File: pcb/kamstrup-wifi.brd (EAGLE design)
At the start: 36 x 42.5 mm, 2 parts

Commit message: pcb: better aligning
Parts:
- moved JP1 9.08 mm to (4.00, 36.3)
- moved U$1 1.80 mm to (5.08, 14.0)
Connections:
- new net N$1: JP1.6, U$1.P$1
- new net N$2: JP1.4, U$1.P$5
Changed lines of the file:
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@@
 <layer number="43" name="vRestrict" color="2" fill="10" visible="yes" active="yes"/>
 <layer number="44" name="Drills" color="7" fill="1" visible="no" active="yes"/>
-<layer number="45" name="Holes" color="7" fill="1" visible="no" active="yes"/>
+<layer number="45" name="Holes" color="7" fill="1" visible="yes" active="yes"/>
 <layer number="46" name="Milling" color="3" fill="1" visible="no" active="yes"/>
 <layer number="47" name="Measures" color="7" fill="1" visible="no" active="yes"/>
@@
 <wire x1="36" y1="42.5" x2="0" y2="42.5" width="0" layer="20"/>
 <wire x1="0" y1="42.5" x2="0" y2="0" width="0" layer="20"/>
-<text x="5.08" y="24.13" size="1.778" layer="1" rot="R90" align="center-right">GND</text>
-<text x="7.62" y="24.13" size="1.778" layer="1" rot="R90" align="center-right">A</text>
-<text x="10.16" y="24.13" size="1.778" layer="1" rot="R90" align="center-right">B</text>
-<text x="5.08" y="31.75" size="1.778" layer="1" rot="R90" align="center-left">VCC</text>
-<text x="7.62" y="31.75" size="1.778" layer="1" rot="R90" align="center-left">TxD</text>
-<text x="10.16" y="31.75" size="1.778" layer="1" rot="R90" align="center-left">RxD</text>
+<text x="1.46" y="32.75" size="0.8128" layer="1" rot="R90" align="center-right">GND</text>
+<text x="4" y="32.75" size="0.8128" layer="1" rot="R90" align="center-right">A</text>
+<text x="6.54" y="32.75" size="0.8128" layer="1" rot="R90" align="center-right">B</text>
+<text x="1.46" y="39.37" size="0.8128" layer="1" rot="R90" align="center-left">VCC</text>
+<text x="4" y="39.37" size="0.8128" layer="1" rot="R90" align="center-left">TxD</text>
+<text x="6.54" y="39.37" size="0.8128" layer="1" rot="R90" align="center-left">RxD</text>
+<hole x="1.5" y="14" drill="2"/>
+<hole x="21.5" y="38.6" drill="2"/>
 </plain>
 <attributes>
@@
 </autorouter>
 <elements>
-<element name="JP1" library="SparkFun-Connectors" package="2X03" value="" x="7.62" y="27.94"/>
-<element name="U$1" library="ESP8266" package="ESP-01" value="ESP8266-01" x="6.35" y="15.24" rot="R270"/>
+<element name="JP1" library="SparkFun-Connectors" package="2X03" value="" x="4" y="36.27"/>
+<element name="U$1" library="ESP8266" package="ESP-01" value="ESP8266-01" x="5.08" y="13.97" rot="R270"/>
 </elements>
 <signals>
@@
 <contactref element="JP1" pad="1"/>
 <contactref element="U$1" pad="P$8"/>
-<wire x1="8.89" y1="15.24" x2="5.08" y2="26.67" width="0" layer="19" extent="1-1"/>
+<wire x1="7.62" y1="13.97" x2="1.46" y2="35" width="0" layer="19" extent="1-1"/>
 </signal>
 <signal name="3.3V">
 <contactref element="JP1" pad="2"/>
 <contactref element="U$1" pad="P$4"/>
-<wire x1="6.35" y1="7.62" x2="5.08" y2="29.21" width="0" layer="19" extent="1-1"/>
+<wire x1="5.08" y1="6.35" x2="1.46" y2="37.54" width="0" layer="19" extent="1-1"/>
+</signal>
+<signal name="N$1">
+<contactref element="U$1" pad="P$1"/>
+<contactref element="JP1" pad="6"/>
+<wire x1="5.08" y1="13.97" x2="6.54" y2="37.54" width="0" layer="19" extent="1-1"/>
+</signal>
+<signal name="N$2">
+<contactref element="JP1" pad="4"/>
+<contactref element="U$1" pad="P$5"/>
+<wire x1="7.62" y1="6.35" x2="4" y2="37.54" width="0" layer="19" extent="1-1"/>
 </signal>
 </signals>

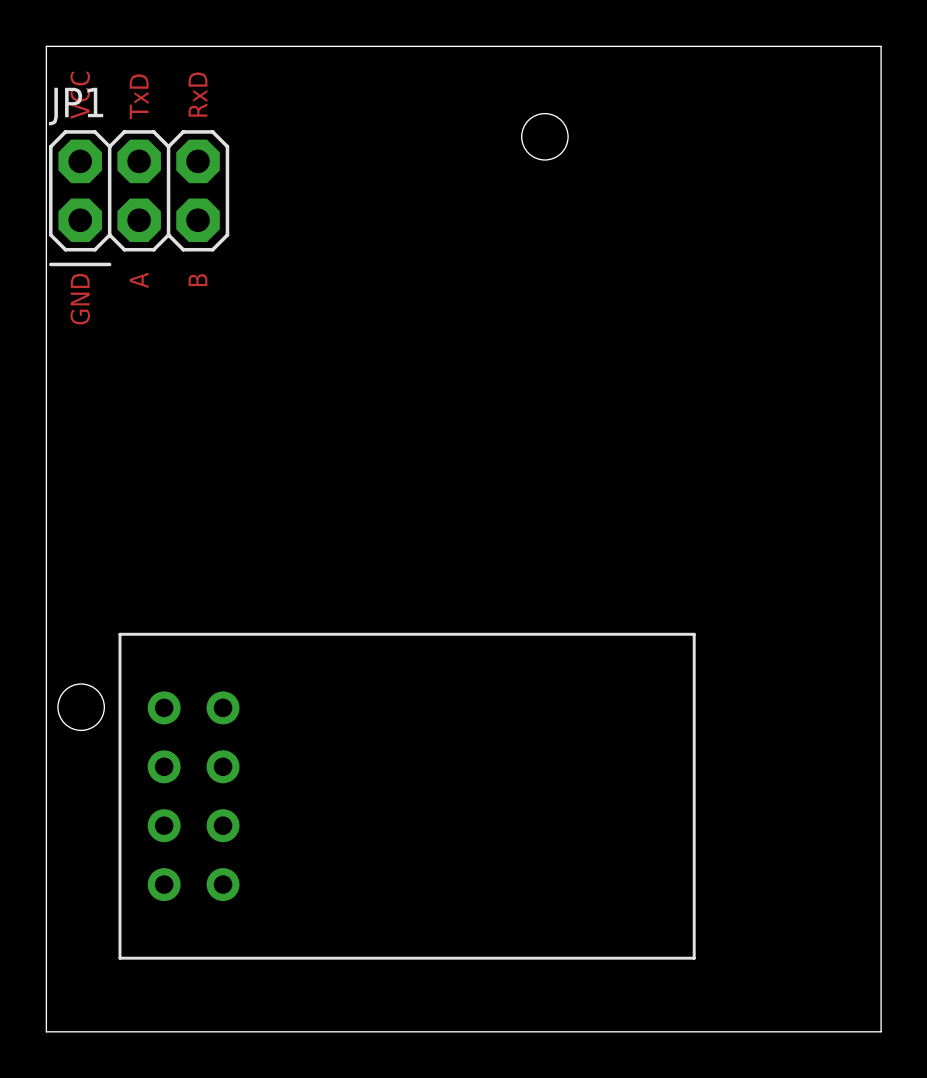
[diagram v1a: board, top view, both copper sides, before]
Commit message: pcb: routing done
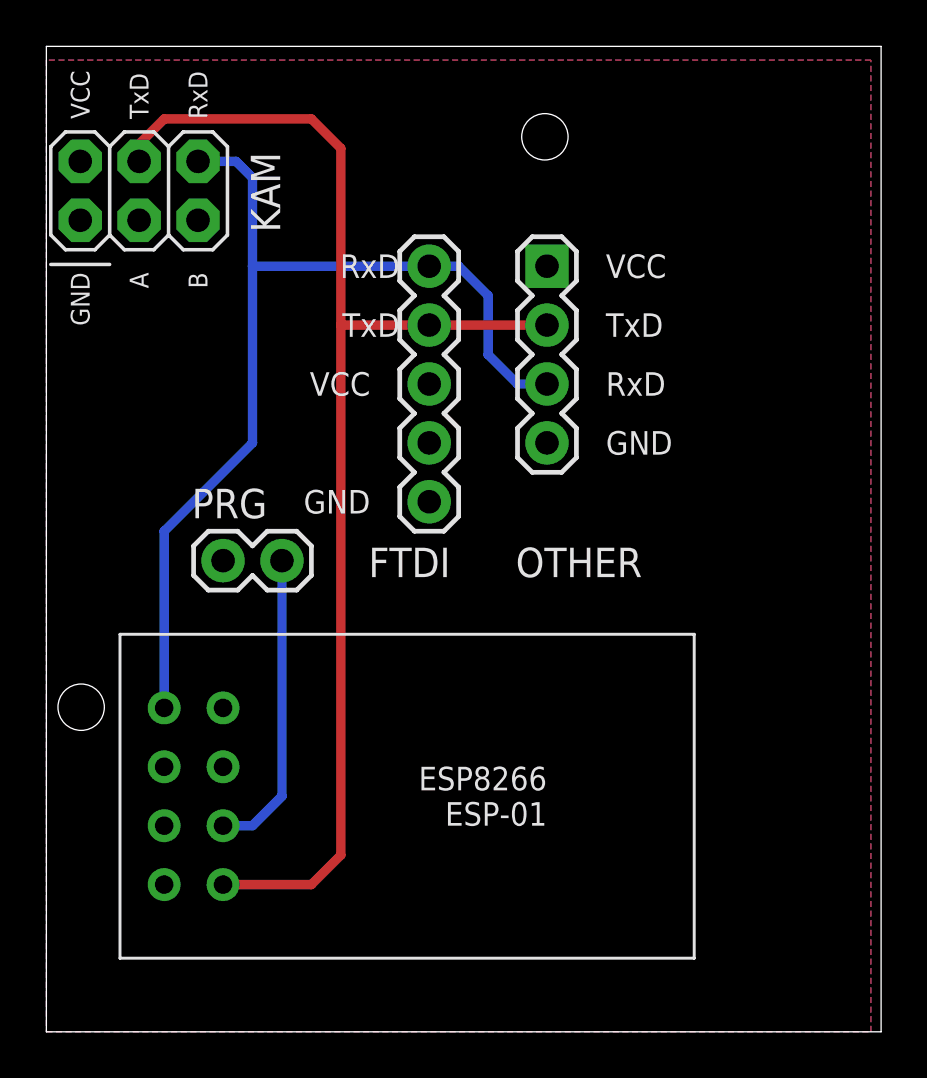
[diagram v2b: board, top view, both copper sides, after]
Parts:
- added FTDI: (no value), SparkFun-Connectors:1X05
- added OTHER: (no value), SparkFun-Connectors:1X04
- added PRG: M02PTH, SparkFun-Connectors:1X02
- renumbered JP1 to KAM
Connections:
- new net N$3: PRG.2, U$1.P$6
- net 3.3V: now also FTDI.3, OTHER.1, U$1.P$2
- net GND: now also FTDI.5, OTHER.4, PRG.1
- net N$1: now also FTDI.1, OTHER.3
- net N$2: now also FTDI.2, OTHER.2
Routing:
- net N$2: track 0.00 -> 55.4 mm
- net N$1: track 0.00 -> 43.4 mm
- net N$3: track 0.00 -> 13.2 mm
- added copper zone on layer 1, net 3.3V
- added copper zone on layer 16, net GND
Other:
- board text added: "ESP8266 ESP-01"

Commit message: pcb: + silk and no cupper under antenna
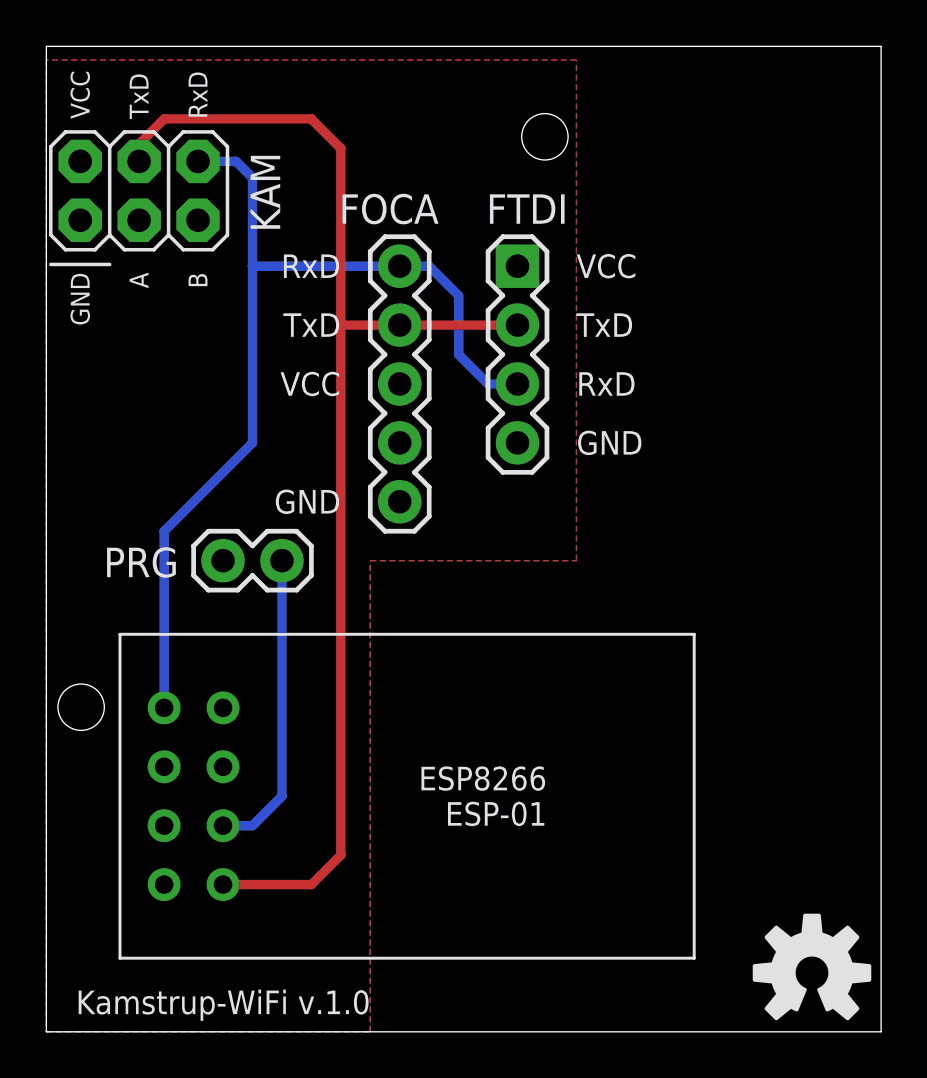
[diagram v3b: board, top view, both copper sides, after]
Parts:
- removed OTHER: (no value), SparkFun-Connectors:1X04
- added FOCA: (no value), SparkFun-Connectors:1X05
- added U$2: (no value), SparkFun-Aesthetics:OSHW-LOGO-M
- FTDI: device SparkFun-Connectors:1X05 -> SparkFun-Connectors:1X04
- moved FTDI 3.81 mm to (20.3, 33.0)
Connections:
- net 3.3V: now also FOCA.3, FTDI.1; no longer FTDI.3, OTHER.1
- net GND: now also FOCA.5, FTDI.4; no longer FTDI.5, OTHER.4
- net N$1: now also FOCA.1, FTDI.3; no longer FTDI.1, OTHER.3
- net N$2: now also FOCA.2; no longer OTHER.2
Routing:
- net N$2: track 55.4 -> 54.1 mm
- net N$1: track 43.4 -> 42.1 mm
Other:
- board text added: "Kamstrup-WiFi v.1.0"
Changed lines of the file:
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@@
 <hole x="1.5" y="14" drill="2"/>
 <hole x="21.5" y="38.6" drill="2"/>
-<text x="24.13" y="33.02" size="1.016" layer="25" align="center-left">VCC</text>
-<text x="24.13" y="30.48" size="1.016" layer="25" align="center-left">TxD</text>
-<text x="24.13" y="27.94" size="1.016" layer="25" align="center-left">RxD</text>
-<text x="24.13" y="25.4" size="1.016" layer="25" align="center-left">GND</text>
-<text x="13.97" y="22.86" size="1.016" layer="25" align="center-right">GND</text>
-<text x="13.97" y="27.94" size="1.016" layer="25" align="center-right">VCC</text>
-<text x="15.24" y="30.48" size="1.016" layer="25" align="center-right">TxD</text>
-<text x="15.24" y="33.02" size="1.016" layer="25" align="center-right">RxD</text>
+<text x="22.86" y="33.02" size="1.016" layer="25" align="center-left">VCC</text>
+<text x="22.86" y="30.48" size="1.016" layer="25" align="center-left">TxD</text>
+<text x="22.86" y="27.94" size="1.016" layer="25" align="center-left">RxD</text>
+<text x="22.86" y="25.4" size="1.016" layer="25" align="center-left">GND</text>
+<text x="12.7" y="22.86" size="1.016" layer="25" align="center-right">GND</text>
+<text x="12.7" y="27.94" size="1.016" layer="25" align="center-right">VCC</text>
+<text x="12.7" y="30.48" size="1.016" layer="25" align="center-right">TxD</text>
+<text x="12.7" y="33.02" size="1.016" layer="25" align="center-right">RxD</text>
 <text x="21.59" y="10.16" size="1.016" layer="25" align="center-right">ESP8266
 ESP-01</text>
+<text x="1.27" y="1.27" size="1.016" layer="25" rot="R180" align="center-right">Kamstrup-WiFi v.1.0</text>
 </plain>
 <attributes>
@@
 </element>
 <element name="U$1" library="ESP8266" package="ESP-01" value="ESP8266-01" x="5.08" y="13.97" rot="R270"/>
-<element name="OTHER" library="SparkFun-Connectors" package="1X04" value="" x="21.59" y="33.02" smashed="yes" rot="R270">
-<attribute name="NAME" x="20.2438" y="19.6088" size="1.27" layer="25" ratio="10"/>
-<attribute name="VALUE" x="18.415" y="34.29" size="1.27" layer="27" rot="R270"/>
-</element>
-<element name="FTDI" library="SparkFun-Connectors" package="1X05" value="" x="16.51" y="33.02" smashed="yes" rot="R270">
-<attribute name="NAME" x="13.8938" y="19.6088" size="1.27" layer="25" ratio="10"/>
-<attribute name="VALUE" x="13.335" y="34.29" size="1.27" layer="27" rot="R270"/>
+<element name="FTDI" library="SparkFun-Connectors" package="1X04" value="" x="20.32" y="33.02" smashed="yes" rot="R270">
+<attribute name="NAME" x="18.9738" y="34.8488" size="1.27" layer="25" ratio="10"/>
+<attribute name="VALUE" x="17.145" y="34.29" size="1.27" layer="27" rot="R270"/>
+</element>
+<element name="FOCA" library="SparkFun-Connectors" package="1X05" value="" x="15.24" y="33.02" smashed="yes" rot="R270">
+<attribute name="NAME" x="12.6238" y="34.8488" size="1.27" layer="25" ratio="10"/>
+<attribute name="VALUE" x="12.065" y="34.29" size="1.27" layer="27" rot="R270"/>
 </element>
 <element name="PRG" library="SparkFun-Connectors" package="1X02" value="M02PTH" x="7.62" y="20.32" smashed="yes">
-<attribute name="NAME" x="6.2738" y="22.1488" size="1.27" layer="25" ratio="10"/>
-</element>
+<attribute name="NAME" x="2.4638" y="19.6088" size="1.27" layer="25" ratio="10"/>
+</element>
+<element name="U$2" library="SparkFun-Aesthetics" package="OSHW-LOGO-M" value="" x="33.02" y="2.54"/>
 </elements>
 <signals>
@@
 <contactref element="KAM" pad="1"/>
 <contactref element="U$1" pad="P$8"/>
-<contactref element="OTHER" pad="4"/>
-<contactref element="FTDI" pad="5"/>
+<contactref element="FTDI" pad="4"/>
+<contactref element="FOCA" pad="5"/>
 <polygon width="0.4064" layer="16" isolate="0.6096">
 <vertex x="0" y="0"/>
-<vertex x="35.56" y="0"/>
-<vertex x="35.56" y="41.91"/>
+<vertex x="13.97" y="0"/>
+<vertex x="13.97" y="20.32"/>
+<vertex x="22.86" y="20.32"/>
+<vertex x="22.86" y="41.91"/>
 <vertex x="0" y="41.91"/>
 </polygon>
@@
 <contactref element="KAM" pad="2"/>
 <contactref element="U$1" pad="P$4"/>
-<contactref element="OTHER" pad="1"/>
-<contactref element="FTDI" pad="3"/>
+<contactref element="FTDI" pad="1"/>
+<contactref element="FOCA" pad="3"/>
 <polygon width="0.4064" layer="1" isolate="0.6096">
 <vertex x="0" y="0"/>
-<vertex x="35.56" y="0"/>
-<vertex x="35.56" y="41.91"/>
+<vertex x="13.97" y="0"/>
+<vertex x="13.97" y="20.32"/>
+<vertex x="22.86" y="20.32"/>
+<vertex x="22.86" y="41.91"/>
 <vertex x="0" y="41.91"/>
 </polygon>
@@
 <contactref element="U$1" pad="P$1"/>
 <contactref element="KAM" pad="6"/>
-<contactref element="OTHER" pad="3"/>
-<contactref element="FTDI" pad="1"/>
-<wire x1="21.59" y1="27.94" x2="20.32" y2="27.94" width="0.4064" layer="16"/>
-<wire x1="20.32" y1="27.94" x2="19.05" y2="29.21" width="0.4064" layer="16"/>
-<wire x1="19.05" y1="29.21" x2="19.05" y2="31.75" width="0.4064" layer="16"/>
-<wire x1="19.05" y1="31.75" x2="17.78" y2="33.02" width="0.4064" layer="16"/>
-<wire x1="17.78" y1="33.02" x2="16.51" y2="33.02" width="0.4064" layer="16"/>
+<contactref element="FTDI" pad="3"/>
+<contactref element="FOCA" pad="1"/>
+<wire x1="20.32" y1="27.94" x2="19.05" y2="27.94" width="0.4064" layer="16"/>
+<wire x1="19.05" y1="27.94" x2="17.78" y2="29.21" width="0.4064" layer="16"/>
+<wire x1="17.78" y1="29.21" x2="17.78" y2="31.75" width="0.4064" layer="16"/>
+<wire x1="17.78" y1="31.75" x2="16.51" y2="33.02" width="0.4064" layer="16"/>
+<wire x1="16.51" y1="33.02" x2="15.24" y2="33.02" width="0.4064" layer="16"/>
 <wire x1="6.54" y1="37.54" x2="8.18" y2="37.54" width="0.4064" layer="16"/>
 <wire x1="8.18" y1="37.54" x2="8.89" y2="36.83" width="0.4064" layer="16"/>
@@
 <wire x1="8.89" y1="25.4" x2="5.08" y2="21.59" width="0.4064" layer="16"/>
 <wire x1="5.08" y1="21.59" x2="5.08" y2="13.97" width="0.4064" layer="16"/>
-<wire x1="16.51" y1="33.02" x2="8.89" y2="33.02" width="0.4064" layer="16"/>
+<wire x1="15.24" y1="33.02" x2="8.89" y2="33.02" width="0.4064" layer="16"/>
 </signal>
 <signal name="N$2">
 <contactref element="KAM" pad="4"/>
 <contactref element="U$1" pad="P$5"/>
-<contactref element="OTHER" pad="2"/>
 <contactref element="FTDI" pad="2"/>
-<wire x1="21.59" y1="30.48" x2="16.51" y2="30.48" width="0.4064" layer="1"/>
+<contactref element="FOCA" pad="2"/>
+<wire x1="20.32" y1="30.48" x2="15.24" y2="30.48" width="0.4064" layer="1"/>
 <wire x1="4" y1="37.54" x2="4" y2="38.29" width="0.4064" layer="1"/>
 <wire x1="4" y1="38.29" x2="5.08" y2="39.37" width="0.4064" layer="1"/>
@@
 <wire x1="12.7" y1="7.62" x2="11.43" y2="6.35" width="0.4064" layer="1"/>
 <wire x1="11.43" y1="6.35" x2="7.62" y2="6.35" width="0.4064" layer="1"/>
-<wire x1="16.51" y1="30.48" x2="12.7" y2="30.48" width="0.4064" layer="1"/>
+<wire x1="15.24" y1="30.48" x2="12.7" y2="30.48" width="0.4064" layer="1"/>
 </signal>
 <signal name="N$3">
